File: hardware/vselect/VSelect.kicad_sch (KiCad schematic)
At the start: 15 parts, among them U1 TPS2113PW

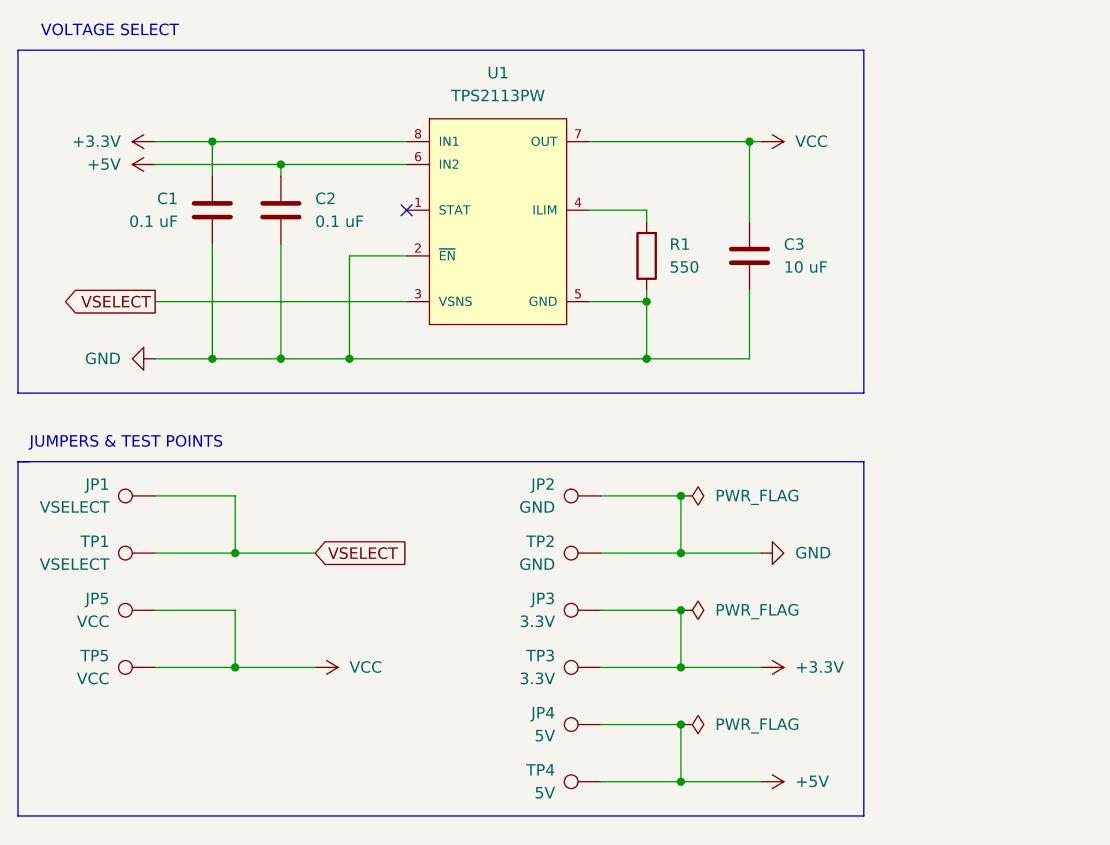
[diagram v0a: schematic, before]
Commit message: VSELECT Module Rev 3
Refreshed things a bit to improve clarity, make installation easier, and to reduce costs when manufacturing in bulk. There is no reason to upgrade already installed modules to this revision.

* Changed the module to be installed on the back of the PCB again as it is much easier to install that way.
* Added pad for the STAT pin. There's no real use for this at the moment.
* Changed the layout slightly to allow room for all of the capacitors' legends. This should make things more clear when assembling a module by hand.
* Changed the legends for the jumper pads to use the net name instead of the designator. This should make things easier during installation.
* Added legends to specify 3.3V/5V for the pads that connect to the power switch footprint. Hopefully, this helps keep people from installing the module incorrectly.
* Updated the TPS2113 footprint to the new one that allows using either the TSSOP or SON package. This should give more flexibility regarding part availability.
* Changed part numbers to more readily available parts. This should reduce the cost of machine assembly.
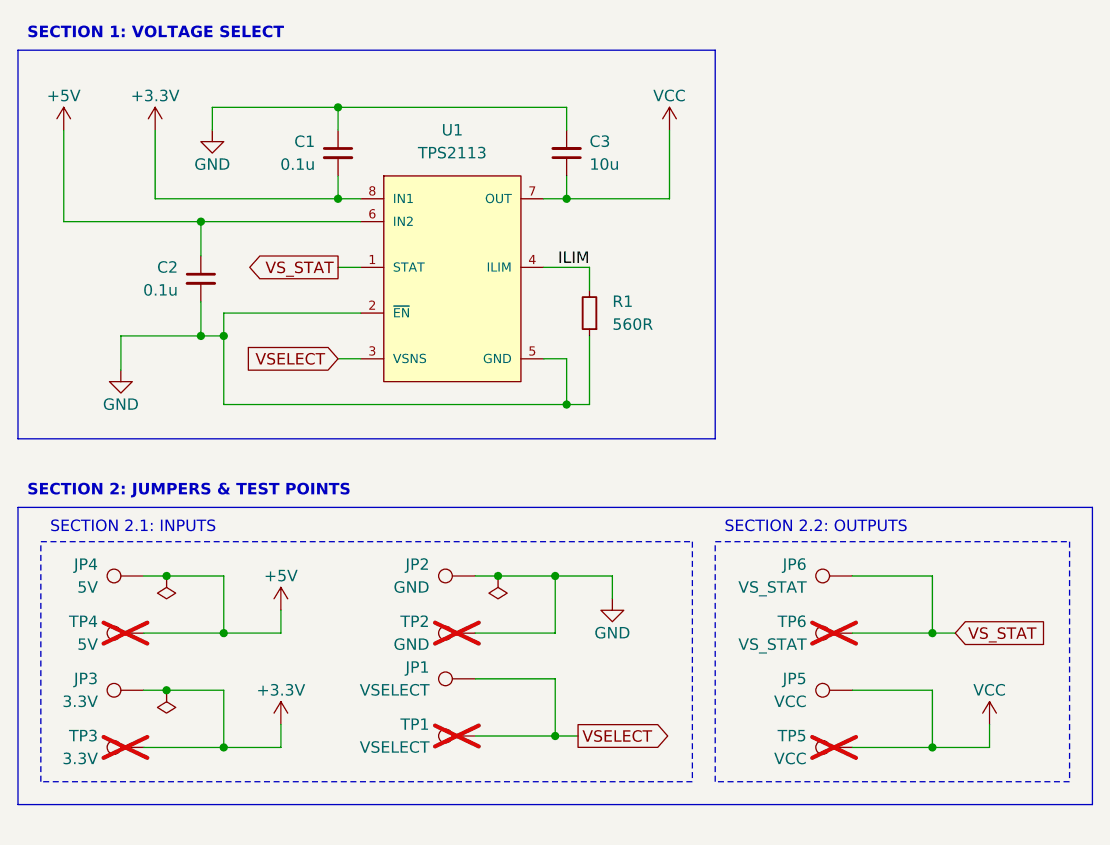
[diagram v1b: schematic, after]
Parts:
- added JP6, TP6: VS_STAT, TestPoint:TestPoint_Pad_2.0x2.0mm, symbol Connector:TestPoint
- C1, C2: value 0.1 uF -> 0.1u; symbol Device:C -> Device:C_Small; JLCPCB C307331 -> C1525; Part (none) -> CL05B104KO5NNNC
- C3: value 10 uF -> 10u; symbol Device:C -> Device:C_Small; Part (none) -> CL05A106MQ5NUNC
- JP1, JP2: now left out of the parts list
- JP3, JP4, JP5: footprint Personal:Vpower-Switch-Pad -> !OSCRMisc:Header - VSELECT - Switch Pad; now left out of the parts list
- R1: value 550 -> 560R; symbol Device:R -> Device:R_Small; Alt Parts (none) -> 1.12A/560R (C137858); 0.98A/510R (C25123); JLCPCB C137858 -> C25123; Note (none) -> The closest JLCPCB "basic part" is for the 510R
- TP1, TP2, TP3, TP4, TP5: now not fitted; now left out of the parts list
- U1: value TPS2113PW -> TPS2113; footprint Personal:Texas_Instruments-TPS2113PW-Level_A -> !OSCRMisc:IC - VSELECT - TPS2113; symbol Added:TPS2113PW -> !OSCRMisc:IC - VSELECT - TPS2113; Code  JEDEC MO-153 -> (none); Datasheet Version SLVS446 -> (none); IN1 IN2 Input VoltageMaxV 5.5 -> (none); IN1 IN2 Input VoltageMinV 2.8 -> (none); IN1 Output CurrentMaxA 1.25 -> (none); IN1 rDSonTypmOhm 84 -> (none); IN2 Output CurrentMaxA 1.25 -> (none); IN2 rDSonTypOhms 0.084 -> (none); LCSC (none) -> C354512; Mounting Technology Surface Mount -> (none); Number of Inputs 2 -> (none); Package Description 8-Pin Plastic Thin Small Outline Package 3 x 4.4 mm Body ,0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 -> (none); Package Version revG, Feb-2011 -> (none); Part (none) -> Hand/TPS2113APWR (C130052); Machine/TPS2113ADRBR (C354512); Sub Family Power Multiplexer (MUX) -> (none); category IC -> (none); ciiva ids 1435368 -> (none); imported yes -> (none); library id 8d418d7fa91867a0 -> (none); manufacturer Texas Instruments -> (none); package PW0008A -> (none); release date 1464590589 -> (none); rohs Yes -> (none); vault revision 9D6D1550-8F4D-4794-945B-26B7B47CC6E6 -> (none)
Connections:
- net GND: now also U1.9 (GND)
- net VS_STAT: now reaches U1.1 (STAT)
- net VS_STAT: now also JP6.1, TP6.1
- net ILIM: now reaches R1.2, U1.4 (ILIM)
- no-connect marks 1 -> 0
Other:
- note removed: "JUMPERS & TEST POINTS"
- note removed: "VOLTAGE SELECT"
- title: (none) -> OSCR Automatic Voltage Selection Module (VSELECT)
- moved on the sheet: C1, C2, C3, JP1, JP2, JP3, JP4, JP5, R1, U1

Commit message: Fix/cleanup the VSELECT Module project files
* Fixed the field name for the LCSC part number so the BOM exports with the part numbers.
* Removed the test points from the schematic as they are no longer needed.
* Added notes for setting the ILIM resistor to the schematic.
* Added an image of the PCB and PDF of the schematic.

Note: The PCB itself didn't change, so it is still Rev 3.
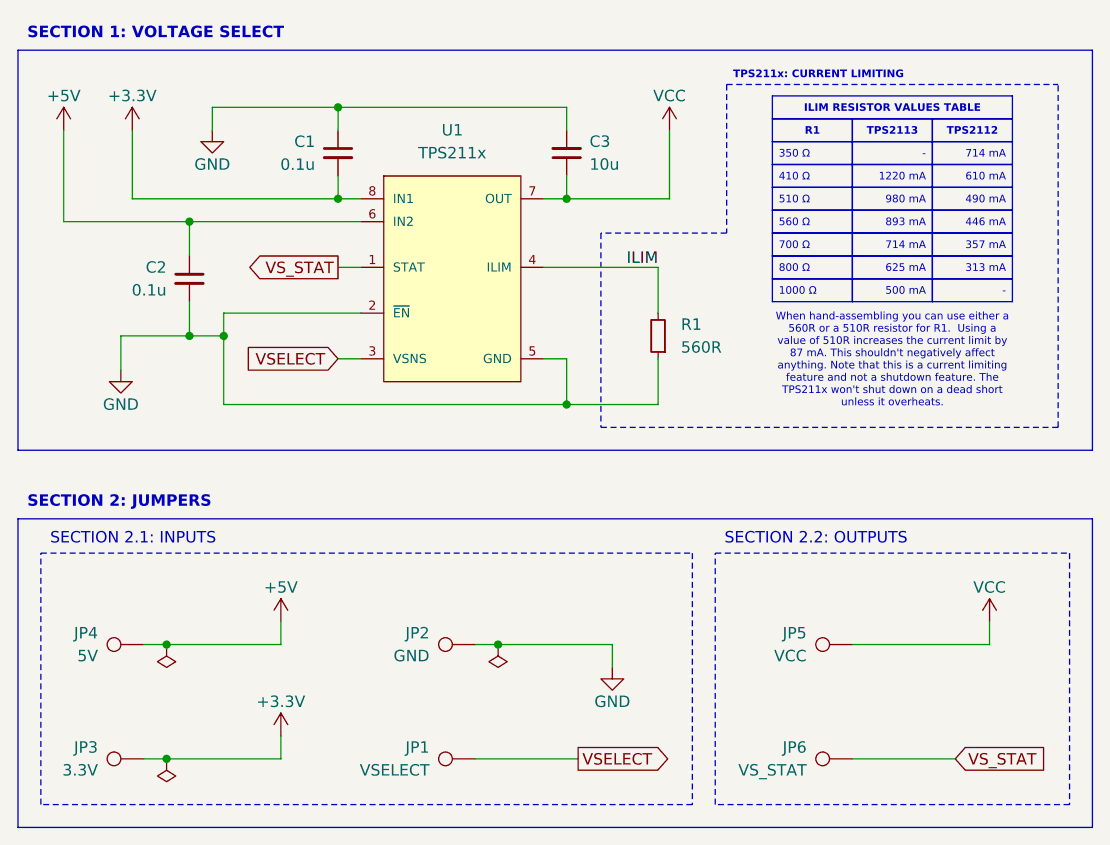
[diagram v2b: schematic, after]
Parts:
- removed TP1: VSELECT, TestPoint:TestPoint_Pad_2.0x2.0mm, symbol Connector:TestPoint
- removed TP2: GND, TestPoint:TestPoint_Pad_2.0x2.0mm, symbol Connector:TestPoint
- removed TP3: 3.3V, TestPoint:TestPoint_Pad_2.0x2.0mm, symbol Connector:TestPoint
- removed TP4: 5V, TestPoint:TestPoint_Pad_2.0x2.0mm, symbol Connector:TestPoint
- removed TP5: VCC, TestPoint:TestPoint_Pad_2.0x2.0mm, symbol Connector:TestPoint
- removed TP6: VS_STAT, TestPoint:TestPoint_Pad_2.0x2.0mm, symbol Connector:TestPoint
- C1, C2: JLCPCB C1525 -> (none); LCSC (none) -> C1525
- C3: JLCPCB C15525 -> (none); LCSC (none) -> C15525
- R1: JLCPCB C25123 -> (none); LCSC (none) -> C25123; Part (none) -> 0402WGF5100TCE
- U1: value TPS2113 -> TPS211x; Note (none) -> You can substitute a TPS2112, just be sure to update the va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
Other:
- moved on the sheet: C2, JP1, JP2, JP3, JP4, JP5, JP6, R1
